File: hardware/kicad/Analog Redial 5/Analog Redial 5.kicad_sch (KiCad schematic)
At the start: 72 parts, among them J1 Barrel_Jack_PTH_Slot, J2 PINHD_1x8_Male, J3 PINHD_1x2_Male, J4 PINHD_1x2_Male, J5 PINHD_2x4_Male, J7 PINHD_1x3_Male, J8 RJ12, J9 RJ12, U1 ESP32-C6-DevKitC-1, U2 ES8388, U3 AG1171, U4 AG1171, U5 XC6206PxxxMR

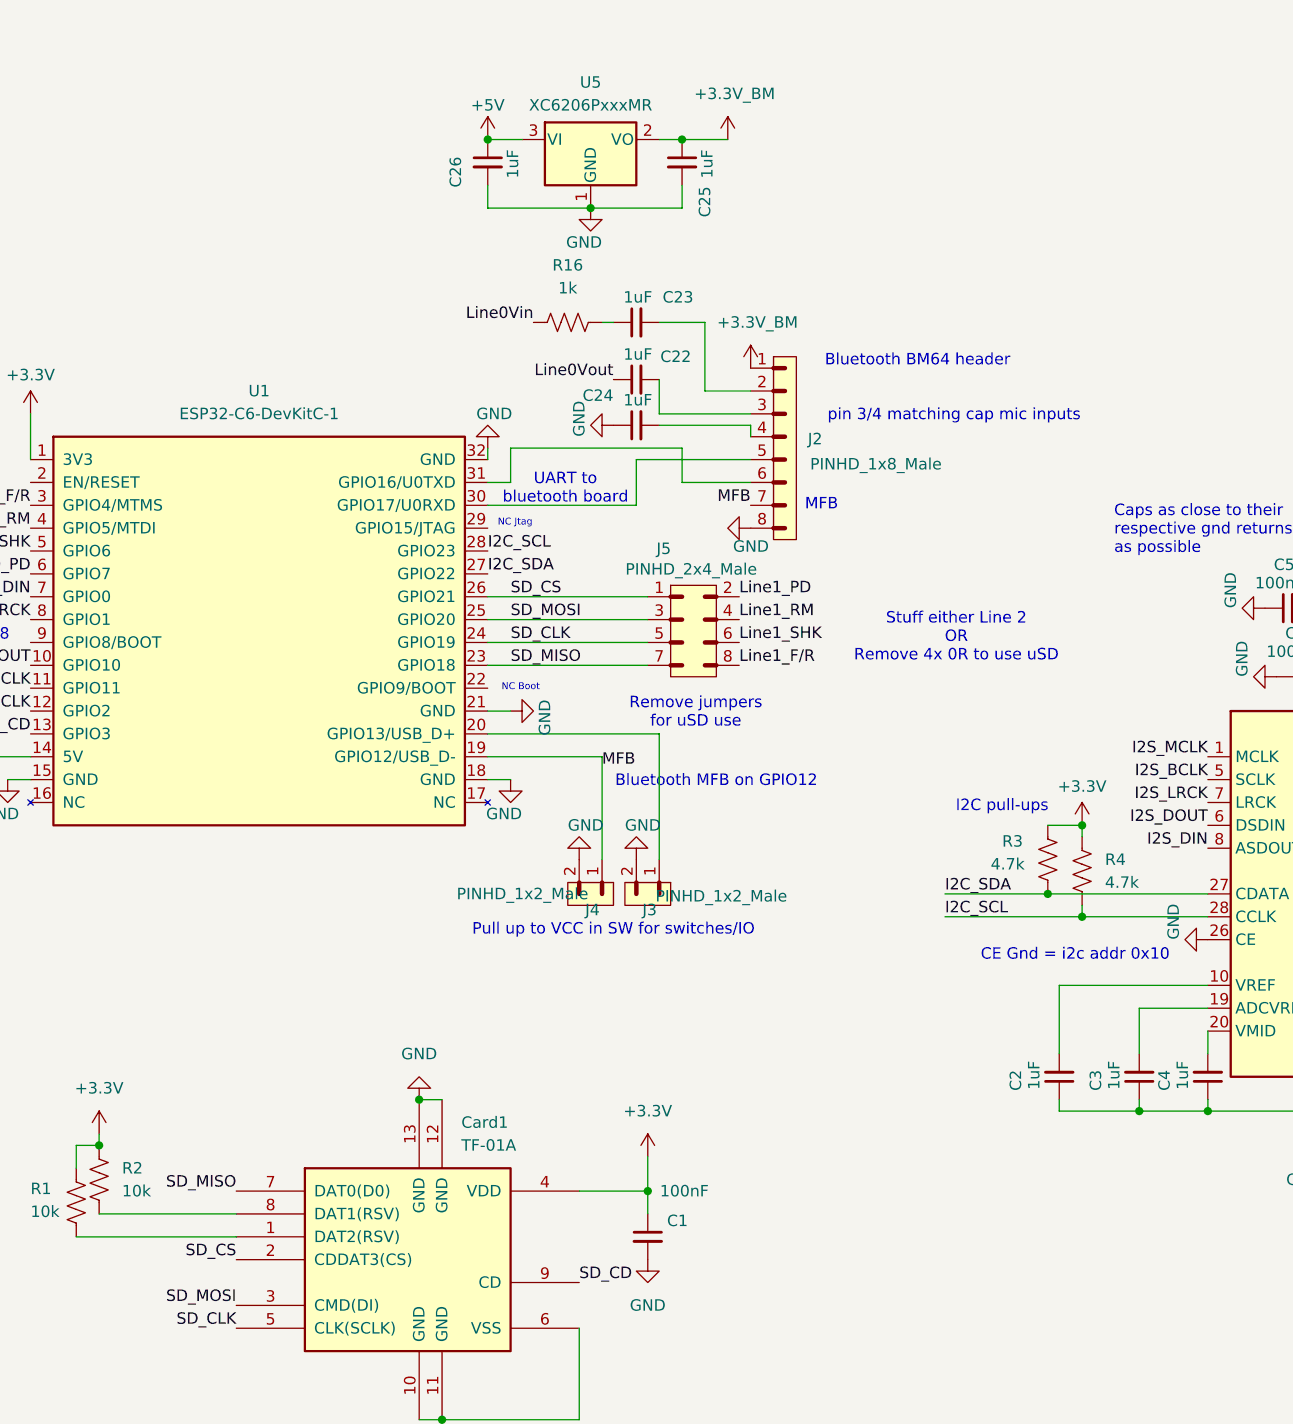
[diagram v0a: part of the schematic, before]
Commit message: SMD5 + BM64 carrier: dedicated 3.3V rail, MFB pin, Vin protection, 8-pin link
Schematic work from the last few sessions' decisions:

SMD5 (Analog Redial 5)
- U5 XC6206P332MR (SOT-23) from +5V with C25/C26 1uF -> new +3V3_BM rail
  feeding the BM64 only, off the DevKit's own 3.3V
- BM64 header J12 -> J2, 6 -> 8 pins: +3V3_BM, AOHPL, MIC_P1, MIC_N1,
  U0RXD, U0TXD, MFB, GND
- MFB on GPIO15 with R17 100k pull-down (it's the BM64's power button --
  held from power-up it master-resets the pairing list)
- R16 1k in series into Line0Vin, and C23 10uF 0805 -> 1uF for the AOHPL
  coupling cap (Vin is 60k, not the few hundred ohms it was sized for)
- C24 1uF from MIC_N1 to GND (the differential mic input's AC ground)
- JP1 placed (Jumper_3_NC-1_Trace) for the planned MCLK/card-detect
  select, not wired yet

BM64 carrier board
- J2 -> J1, 8-pin socket mirroring the new SMD5 header, adding MIC_N1 and
  MFB
- New J2, 4-pin: P2_0 / RST_N / MFB, the one-time EEPROM-programming
  header that mates to J5 (replaces the loose J6/J10/J11 jumpers)

Co-Authored-By: Claude Opus 5 <noreply@anthropic.com>
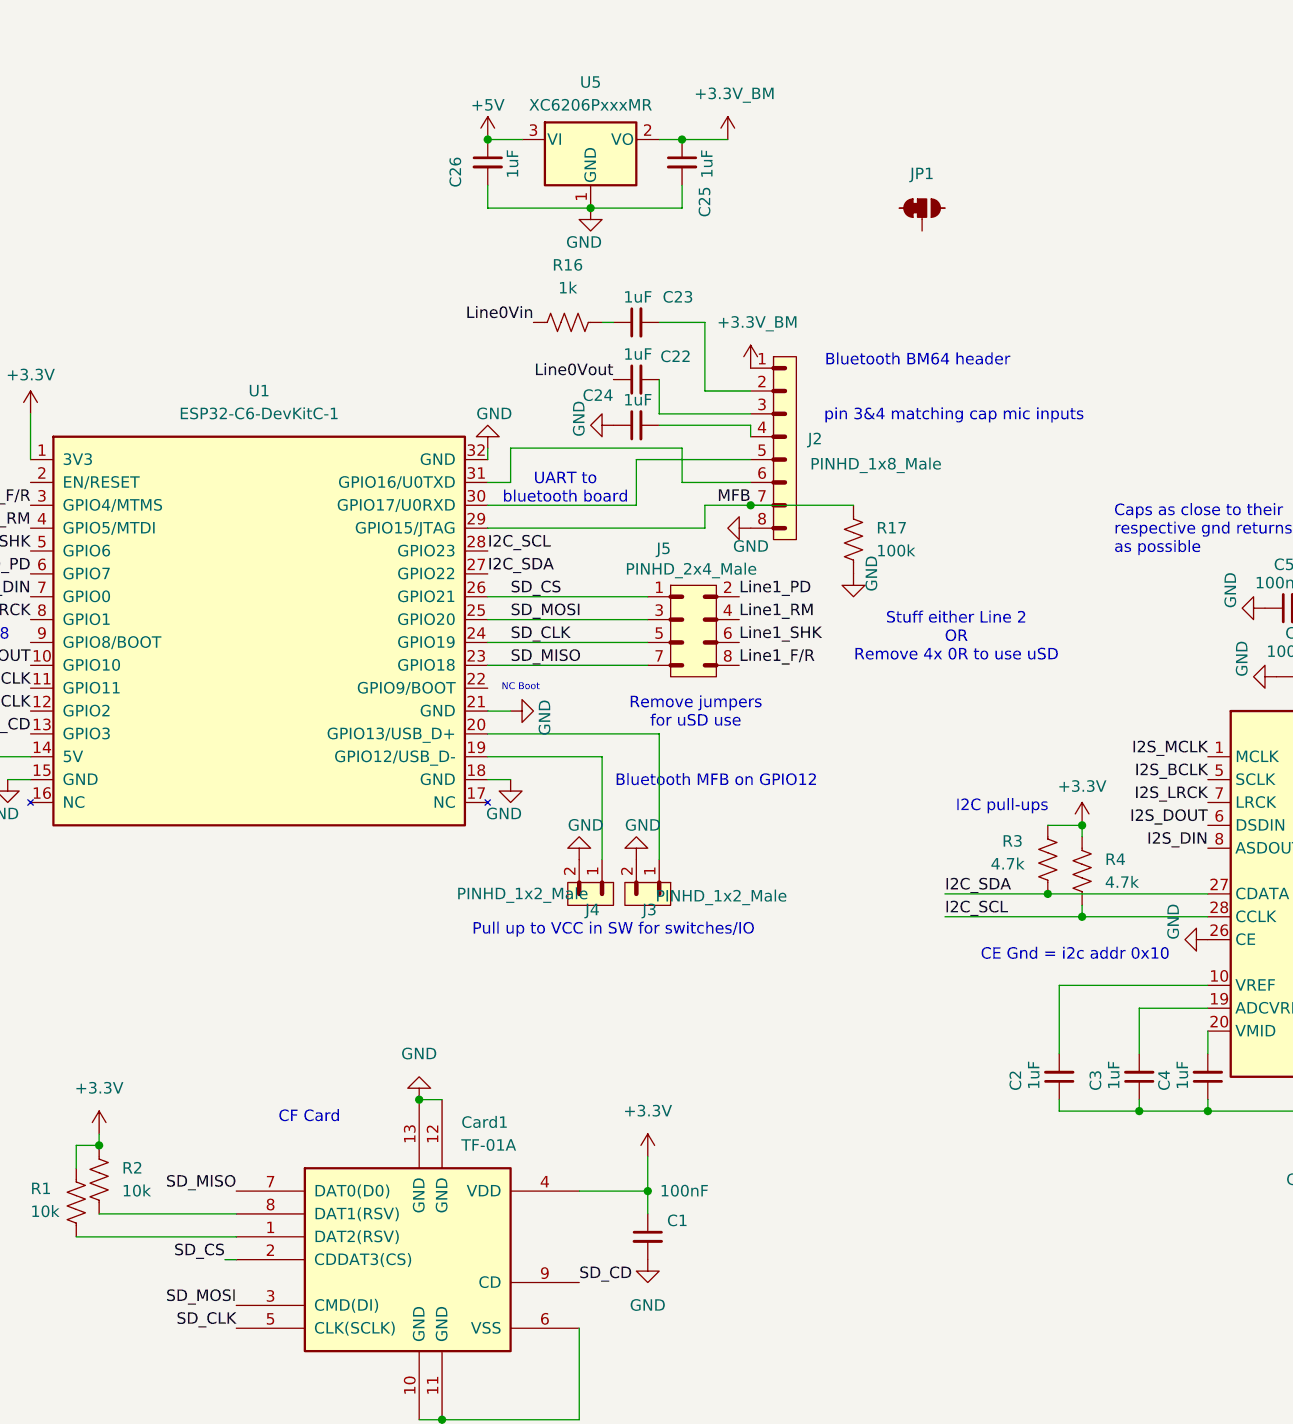
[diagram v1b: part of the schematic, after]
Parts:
- added JP1: (no value), PCM_SparkFun-Jumper:Jumper_3_NC-1_Trace_NoSilk, symbol PCM_SparkFun-Jumper:SolderJumper_3_Bridged12_No_Silk
- added R17: 100k, Resistor_SMD:R_0402_1005Metric, symbol PCM_SparkFun-Resistor:R
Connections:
- net GND: now also R17.1
- net MFB: now also U1.29 (GPIO15/JTAG), R17.2; no longer J4.1, U1.19 (GPIO12/USB_D-)
- new net: J4.1, U1.19 (GPIO12/USB_D-)
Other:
- note added: "CF Card"
- note added: "pin 3&4 matching cap mic inputs"
- note removed: "MFB"
- note removed: "NC Jtag"
- note removed: "pin 3/4 matching cap mic inputs"

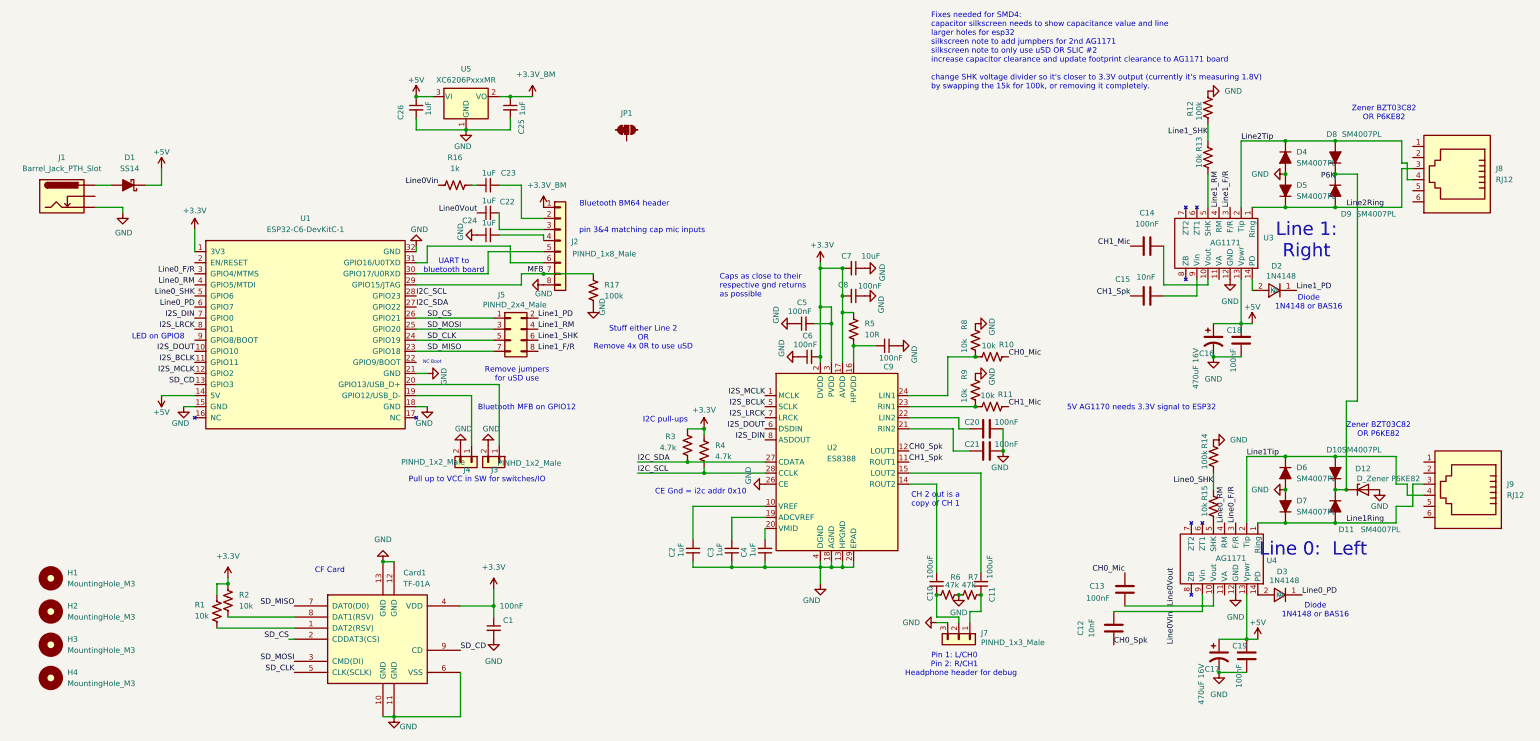
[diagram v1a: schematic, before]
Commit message: SMD5 + carrier: solder jumpers, C10/C11 to a disc footprint, 2-pin programming header
- SMD5: JP2/JP3 solder jumpers placed; C10/C11 100 uF 1206 -> 47 uF on
  Capacitor_THT:C_Disc_D4.7mm_W2.5mm_P5.00mm (DNP, fit 1 uF to use J7)
- Carrier: programming header down to 2 pins (P2_0, RST_N) now that MFB
  reaches the module through the main 8-pin link -- this also removes the
  hazard of MFB being driven from two connectors at once
- Cross-reference fixes missed by the hardware-doc split commit
- .gitignore: the Bluetooth carrier lives outside hardware/kicad/, so repeat
  the jlcpcb/, production_files/, tmp*.rpt and _restore_backup_* rules there

KNOWN ISSUE, not fixed here: carrier J1 pins 2 and 3 are swapped, so ESP TX
meets BM64 TX and ESP RX meets BM64 RX. See the next commit.

Co-Authored-By: Claude Opus 5 <noreply@anthropic.com>
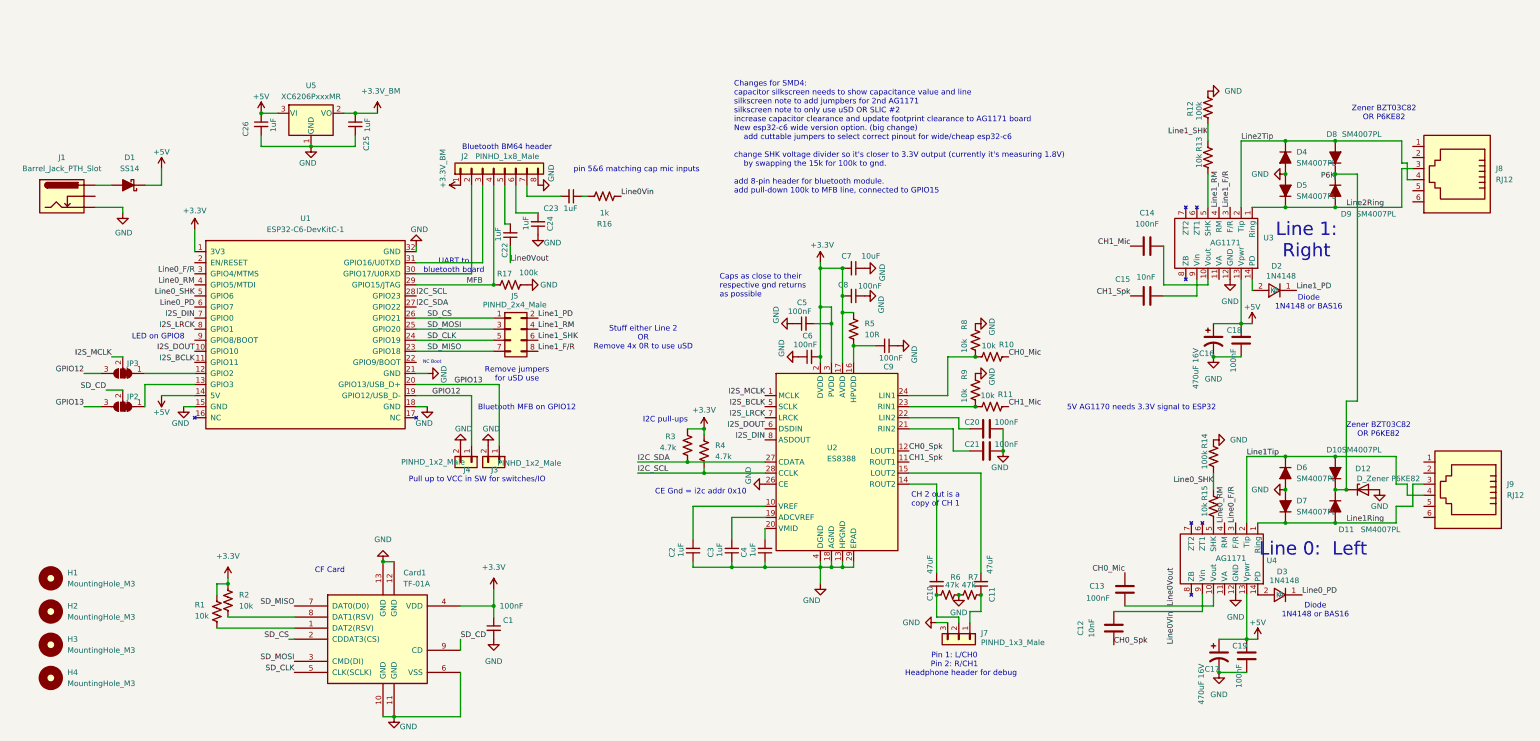
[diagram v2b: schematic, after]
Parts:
- removed JP1: (no value), PCM_SparkFun-Jumper:Jumper_3_NC-1_Trace_NoSilk, symbol PCM_SparkFun-Jumper:SolderJumper_3_Bridged12_No_Silk
- added JP2, JP3: (no value), PCM_SparkFun-Jumper:Jumper_3_NC-1_Trace_NoSilk, symbol Jumper:SolderJumper_3_Bridged12
- C10, C11: value 100uF -> 47uF; footprint Capacitor_SMD:C_1206_3216Metric -> Capacitor_THT:C_Disc_D4.7mm_W2.5mm_P5.00mm
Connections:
- net I2S_MCLK: now also JP3.2 (C); no longer U1.12 (GPIO2)
- net MFB: now also J2.4; no longer J2.7
- net SD_CD: now also JP2.2 (C); no longer U1.13 (GPIO3)
- net GPIO12: now reaches J4.1, U1.19 (GPIO12/USB_D-)
- net GPIO12: now also JP3.3 (B)
- net at C24.2: now also J2.6; no longer J2.4
- net at C23.2: now also J2.7; no longer J2.2
- net GPIO13: now reaches J3.1, U1.20 (GPIO13/USB_D+)
- net GPIO13: now also JP2.3 (B)
- net at U1.30 (GPIO17/U0RXD): now also J2.2; no longer J2.5
- net at U1.31 (GPIO16/U0TXD): now also J2.3; no longer J2.6
- net at C22.2: now also J2.5; no longer J2.3
- new net: JP3.1 (A), U1.12 (GPIO2)
- new net: JP2.1 (A), U1.13 (GPIO3)
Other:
- note added: "Changes for SMD4: capacitor silkscreen needs to show capacitance value and line silkscreen note to add jumpbers for 2nd AG1171 silkscreen note to only use uSD OR SLIC #2 increase capacitor clearance and update footprint clearance to AG1171 board New esp32-c6 wide version option. (big change) add cuttable jumpers to select correct pinout for wide/cheap esp32-c6 change SHK voltage divider so it's c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"
- note added: "pin 5&6 matching cap mic inputs"
- note removed: "Fixes needed for SMD4: capacitor silkscreen needs to show capacitance value and line larger holes for esp32 silkscreen note to add jumpbers for 2nd AG1171 silkscreen note to only use uSD OR SLIC #2 increase capacitor clearance and update footprint clearance to AG1171 board change SHK voltage divider so it's closer to 3.3V output (currently it's measuring 1.8V) by swapping the 15k for 100k, or rem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"
- note removed: "pin 3&4 matching cap mic inputs"
- moved on the sheet: C22, C23, C24, C25, C26, J2, R16, R17, U5

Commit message: kicad: consolidate custom footprints/3D/symbols into libraries/
Move all per-project Scott.pretty, JLCImport.pretty, .3dshapes, and
.kicad_sym files into a single shared kicad/libraries/ directory.
Rename "Scott" library to "Custom" throughout. Update fp-lib-table,
sym-lib-table, .kicad_pcb, and .kicad_sch files in all 6 board
projects to resolve Custom: and JLCImport: via ${KIPRJMOD}/../libraries/.

Also fixes broken 3D model paths (hardcoded /Users/... and
_restore_backup_ references in SMD3/SMD4/AR5 PCBs).

Generated with [Devin](https://devin.ai)

Co-Authored-By: Devin <158243242+devin-ai-integration[bot]@users.noreply.github.com>
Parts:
- J8, J9: footprint Scott:RJ12_Amphenol_87180_Horizontal -> Custom:RJ12_Amphenol_87180_Horizontal
- U1: footprint Scott:ESP32-C6-DevKitC-dual -> Custom:ESP32-C6-DevKitC-dual
- U3, U4: footprint Scott:AG1171_SIL -> Custom:AG1171_SIL; symbol Scott_Symbol_Library:AG1171_SIL -> Custom_Symbol_Library:AG1171_SIL
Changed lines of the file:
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@@
 			)
 		)
-		(property "Footprint" "Scott:RJ12_Amphenol_87180_Horizontal"
+		(property "Footprint" "Custom:RJ12_Amphenol_87180_Horizontal"
 			(at 364.49 67.945 90)
 			(hide yes)
@@
 			)
 		)
-		(property "Footprint" "Scott:RJ12_Amphenol_87180_Horizontal"
+		(property "Footprint" "Custom:RJ12_Amphenol_87180_Horizontal"
 			(at 367.03 140.335 90)
 			(hide yes)
@@
 			)
 		)
-		(property "Footprint" "Scott:ESP32-C6-DevKitC-dual"
+		(property "Footprint" "Custom:ESP32-C6-DevKitC-dual"
 			(at 100.33 129.54 0)
 			(hide yes)
@@
 	)
 	(symbol
-		(lib_id "Scott_Symbol_Library:AG1171_SIL")
+		(lib_id "Custom_Symbol_Library:AG1171_SIL")
 		(at 308.61 160.02 180)
 		(unit 1)
@@
 			)
 		)
-		(property "Footprint" "Scott:AG1171_SIL"
+		(property "Footprint" "Custom:AG1171_SIL"
 			(at 308.61 160.02 0)
 			(hide yes)
@@
 	)
 	(symbol
-		(lib_id "Scott_Symbol_Library:AG1171_SIL")
+		(lib_id "Custom_Symbol_Library:AG1171_SIL")
 		(at 307.34 87.63 180)
 		(unit 1)
@@
 			)
 		)
-		(property "Footprint" "Scott:AG1171_SIL"
+		(property "Footprint" "Custom:AG1171_SIL"
 			(at 307.34 87.63 0)
 			(hide yes)

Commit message: Archive the superseded KiCad projects; LDO value; feature-ideas notebook
- hardware/kicad/{Rotary_phone_SMD3,Rotary_phone_SMD_old,rotary_phone_gateway}
  move under hardware/kicad/Old/ -- all 50 files verified present at the new
  path before committing the deletions
- SMD5: U5 value XC6206PxxxMR -> XC6206P332MR (the 3.3 V part actually
  ordered, LCSC C5446)
- archive/FEATURE_IDEAS.md: running list of ideas worth keeping out of chat
  history, starting with in-call DTMF feature codes

Co-Authored-By: Claude Opus 5 <noreply@anthropic.com>
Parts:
- U5: value XC6206PxxxMR -> XC6206P332MR
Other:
- note removed: "Bluetooth MFB on GPIO12"
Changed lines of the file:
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@@
 		)
 	)
-	(text "Bluetooth MFB on GPIO12"
-		(exclude_from_sim no)
-		(at 151.13 122.174 0)
-		(effects
-			(font
-				(size 1.27 1.27)
-			)
-		)
-	)
 	(text "Remove jumpers\nfor uSD use"
 		(exclude_from_sim no)
@@
 		)
 	)
-	(text "Changes for SMD4:\ncapacitor silkscreen needs to show capacitance value and line\nsilkscreen note to add jumpbers for 2nd AG1171\nsilkscreen note to only use uSD OR SLIC #2\nincrease capacitor clearance and update footprint clearance to AG1171 board\nNew esp32-c6 wide version option. (big change)\n	add cuttable jumpers to select correct pinout for wide/cheap esp32-c6\n\nchange SHK voltage divider so it's closer to 3.3V output (currently it's measuring 1.8V)\n	by swapping the 15k for 100k to gnd.\n\nadd 8-pin header for bluetooth module.\nadd pull-down 100k to MFB line, connected to GPIO15\n\n"
+	(text "Changes for SMD4:\ncapacitor silkscreen needs to show capacitance value and line\nsilkscreen note to add jumpbers for 2nd AG1171\nsilkscreen note to only use uSD OR SLIC #2\nincrease capacitor clearance and update footprint clearance to AG1171 board\nNew esp32-c6 wide version option. (big change)\n	add cuttable jumpers to select correct pinout for wide/cheap esp32-c6\n\nchange SHK voltage divider so it's closer to 3.3V output (currently it's measuring 1.8V)\n	by swapping the 15k for 100k to gnd.\n\nadd 8-pin header for bluetooth module.\nadd pull-down 100k to MFB line, connected to GPIO15\nAdd 3.3V regulator for optional bluetooth module\n\n"
 		(exclude_from_sim no)
 		(at 198.628 61.214 0)
@@
 			)
 		)
-		(property "Value" "XC6206PxxxMR"
+		(property "Value" "XC6206P332MR"
 			(at 101.6 50.8 0)
 			(show_name no)
